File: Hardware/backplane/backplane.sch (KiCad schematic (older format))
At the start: 45 parts, among them J1 USB_B_Micro, SW1 SW_SPST, U2 MAX811SEUS-T, U3 MAX811SEUS-T, U4 PAL24, X1 CXO_DIP8

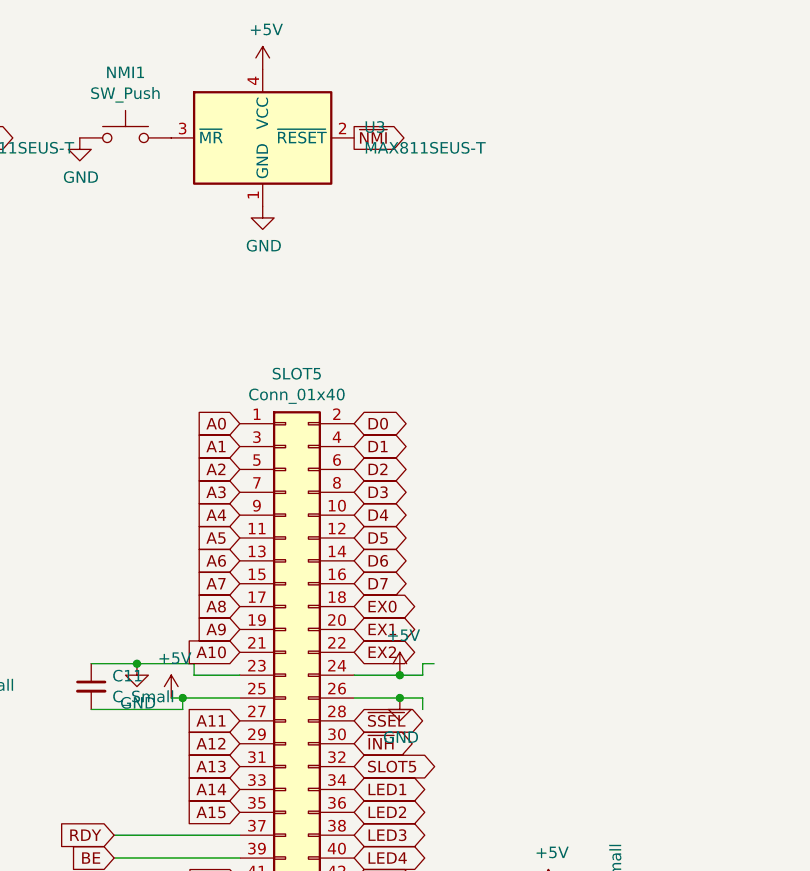
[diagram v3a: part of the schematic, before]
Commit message: Add resistor between output of NMI MAX811 and NMI line to enable NMI to be controlled from the bus
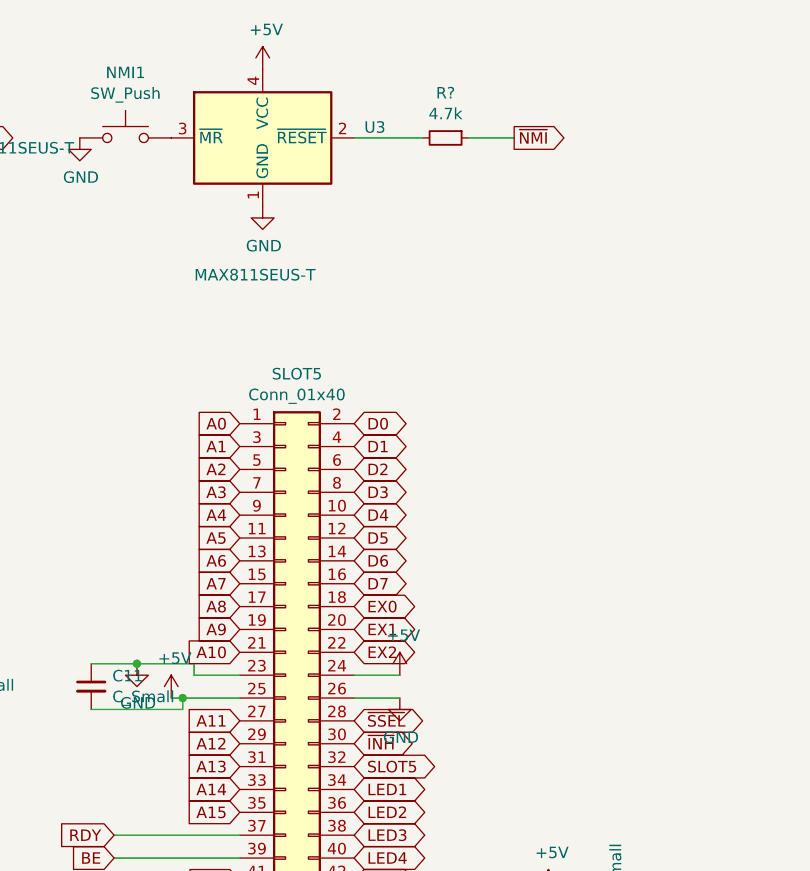
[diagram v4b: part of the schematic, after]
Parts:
- added R?: 4.7k, Resistor_SMD:R_0805_2012Metric_Pad1.15x1.40mm_HandSolder, symbol Device:R_Small
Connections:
- wire segments 123 -> 120
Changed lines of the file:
@@
 Text GLabel 8200 4550 0    50   Input ~ 0
 ~IRQ~
-Wire Wire Line
-	9600 3400 9550 3400
-Wire Wire Line
-	9550 3400 9550 3450
-Wire Wire Line
-	9550 3450 9450 3450
-Connection ~ 9450 3450
-Wire Wire Line
-	9550 3600 9550 3550
-Wire Wire Line
-	9550 3550 9450 3550
-Connection ~ 9450 3550
 $Comp
 L Device:C_Small C11
@@
 P 8850 1100
 F 0 "U3" H 9294 1146 50  0000 L CNN
-F 1 "MAX811SEUS-T" H 9294 1055 50  0000 L CNN
+F 1 "MAX811SEUS-T" H 8550 500 50  0000 L CNN
 F 2 "Package_TO_SOT_SMD:SOT-143" H 8950 800 50  0001 L CNN
 F 3 "https://datasheets.maximintegrated.com/en/ds/MAX811-MAX812.pdf" H 8500 400 50  0001 C CNN
@@
 	1    0    0    -1
 $EndComp
-Text GLabel 9250 1100 2    50   Output ~ 0
+Text GLabel 9950 1100 2    50   Output ~ 0
 ~NMI~
 Text GLabel 7450 1100 2    50   Output ~ 0
@@
 Wire Wire Line
 	1550 1100 2050 1100
+Wire Wire Line
+	9950 1100 9750 1100
+Wire Wire Line
+	9550 1100 9250 1100
+$Comp
+L Device:R_Small R?
+U 1 1 60052F9C
+P 9650 1100
+F 0 "R?" V 9454 1100 50  0000 C CNN
+F 1 "4.7k" V 9545 1100 50  0000 C CNN
+F 2 "Resistor_SMD:R_0805_2012Metric_Pad1.15x1.40mm_HandSolder" H 9650 1100 50  0001 C CNN
+F 3 "~" H 9650 1100 50  0001 C CNN
+	1    9650 1100
+	0    1    1    0
+$EndComp
 $EndSCHEMATC

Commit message: change resistor
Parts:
- gave numbers to parts that had none: 1
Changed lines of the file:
@@
 	9550 1100 9250 1100
 $Comp
-L Device:R_Small R?
+L Device:R_Small R16
 U 1 1 60052F9C
 P 9650 1100
-F 0 "R?" V 9454 1100 50  0000 C CNN
+F 0 "R16" V 9454 1100 50  0000 C CNN
 F 1 "4.7k" V 9545 1100 50  0000 C CNN
 F 2 "Resistor_SMD:R_0805_2012Metric_Pad1.15x1.40mm_HandSolder" H 9650 1100 50  0001 C CNN

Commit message: Add backplane gerbers
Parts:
- removed C2: C_Small, Capacitor_SMD:C_1206_3216Metric_Pad1.42x1.75mm_HandSolder, symbol Device:C_Small
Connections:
- wire segments 120 -> 114
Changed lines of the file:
@@
 ~IRQ~
-$Comp
-L Device:C_Small C2
-U 1 1 5FD8A65F
-P 3150 3500
-F 0 "C2" H 3242 3546 50  0000 L CNN
-F 1 "C_Small" H 3242 3455 50  0000 L CNN
-F 2 "Capacitor_SMD:C_1206_3216Metric_Pad1.42x1.75mm_HandSolder" H 3150 3500 50  0001 C CNN
-F 3 "~" H 3150 3500 50  0001 C CNN
-	1    3150 3500
-	1    0    0    -1
-$EndComp
-Wire Wire Line
-	3150 3400 3100 3400
-Wire Wire Line
-	3100 3400 3100 3450
-Wire Wire Line
-	3100 3450 3000 3450
-Connection ~ 3000 3450
-Wire Wire Line
-	3150 3600 3100 3600
-Wire Wire Line
-	3100 3600 3100 3550
-Wire Wire Line
-	3100 3550 3000 3550
-Connection ~ 3000 3550
 $Comp
 L Device:C_Small C1
@@
 	1    0    0    -1
 $EndComp
-Text GLabel 10700 5050 2    50   Output ~ 0
+Text GLabel 10700 5850 2    50   Output ~ 0
 CLK
 Text GLabel 4950 3650 2    50   BiDi ~ 0

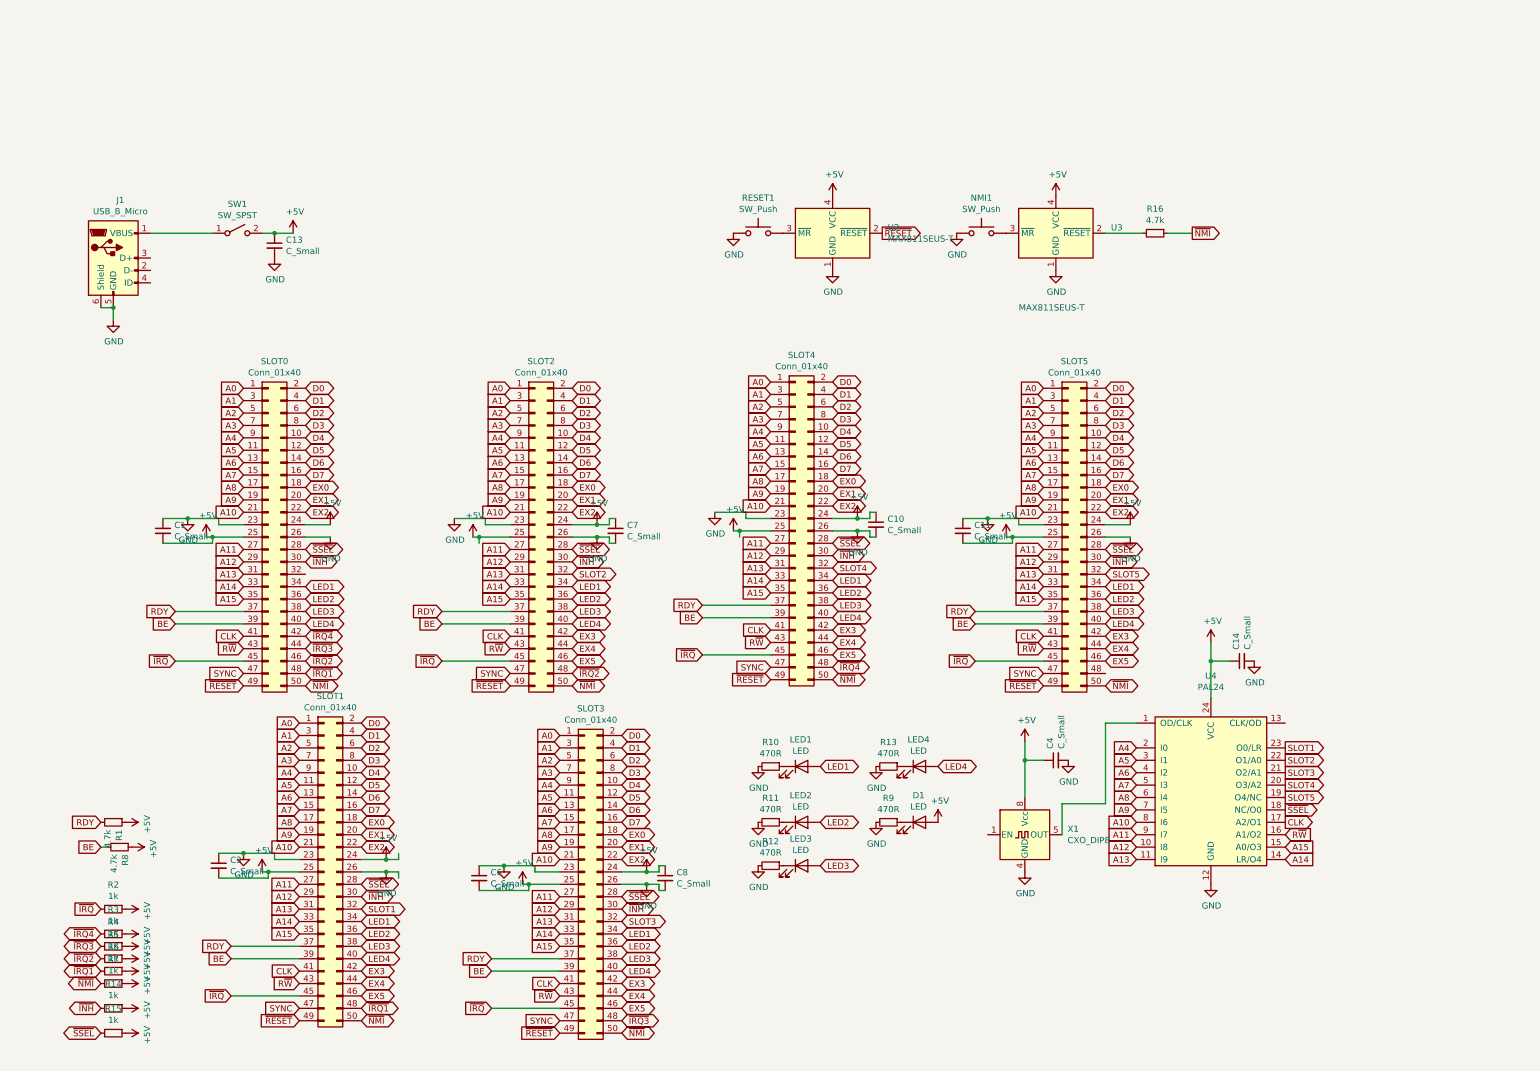
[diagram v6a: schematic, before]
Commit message: Add clock stretching with counter and slow clock request from peripherals.
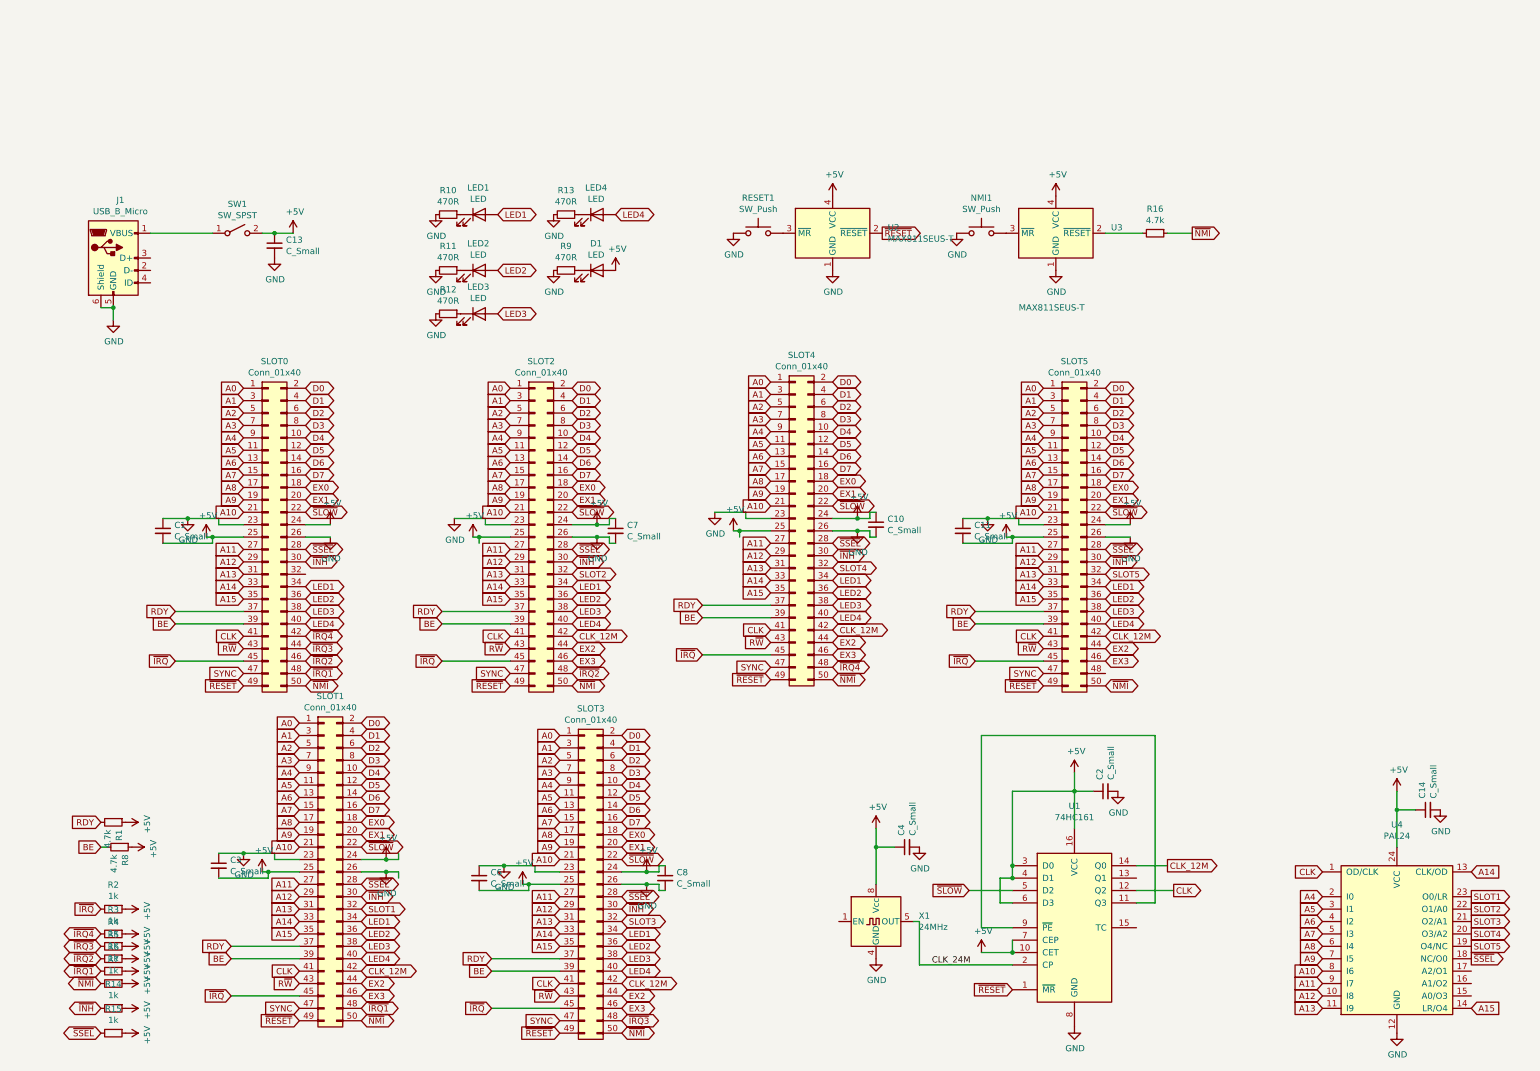
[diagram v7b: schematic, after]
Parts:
- added C2: C_Small, Capacitor_SMD:C_1206_3216Metric_Pad1.42x1.75mm_HandSolder, symbol Device:C_Small
- added U1: 74HC161, Package_DIP:DIP-16_W7.62mm_Socket, symbol 74xx:74LS161
- X1: value CXO_DIP8 -> 24MHz
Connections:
- net labels added: CLK_12M, CLK_24M, ~SLOW~
- net labels removed: EX4, EX5
- wire segments 114 -> 132
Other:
- moved on the sheet: C14, C4, D1, LED1, LED2, LED3, LED4, R10, R11, R12, R13, R9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

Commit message: each slot gets it's own slow signal
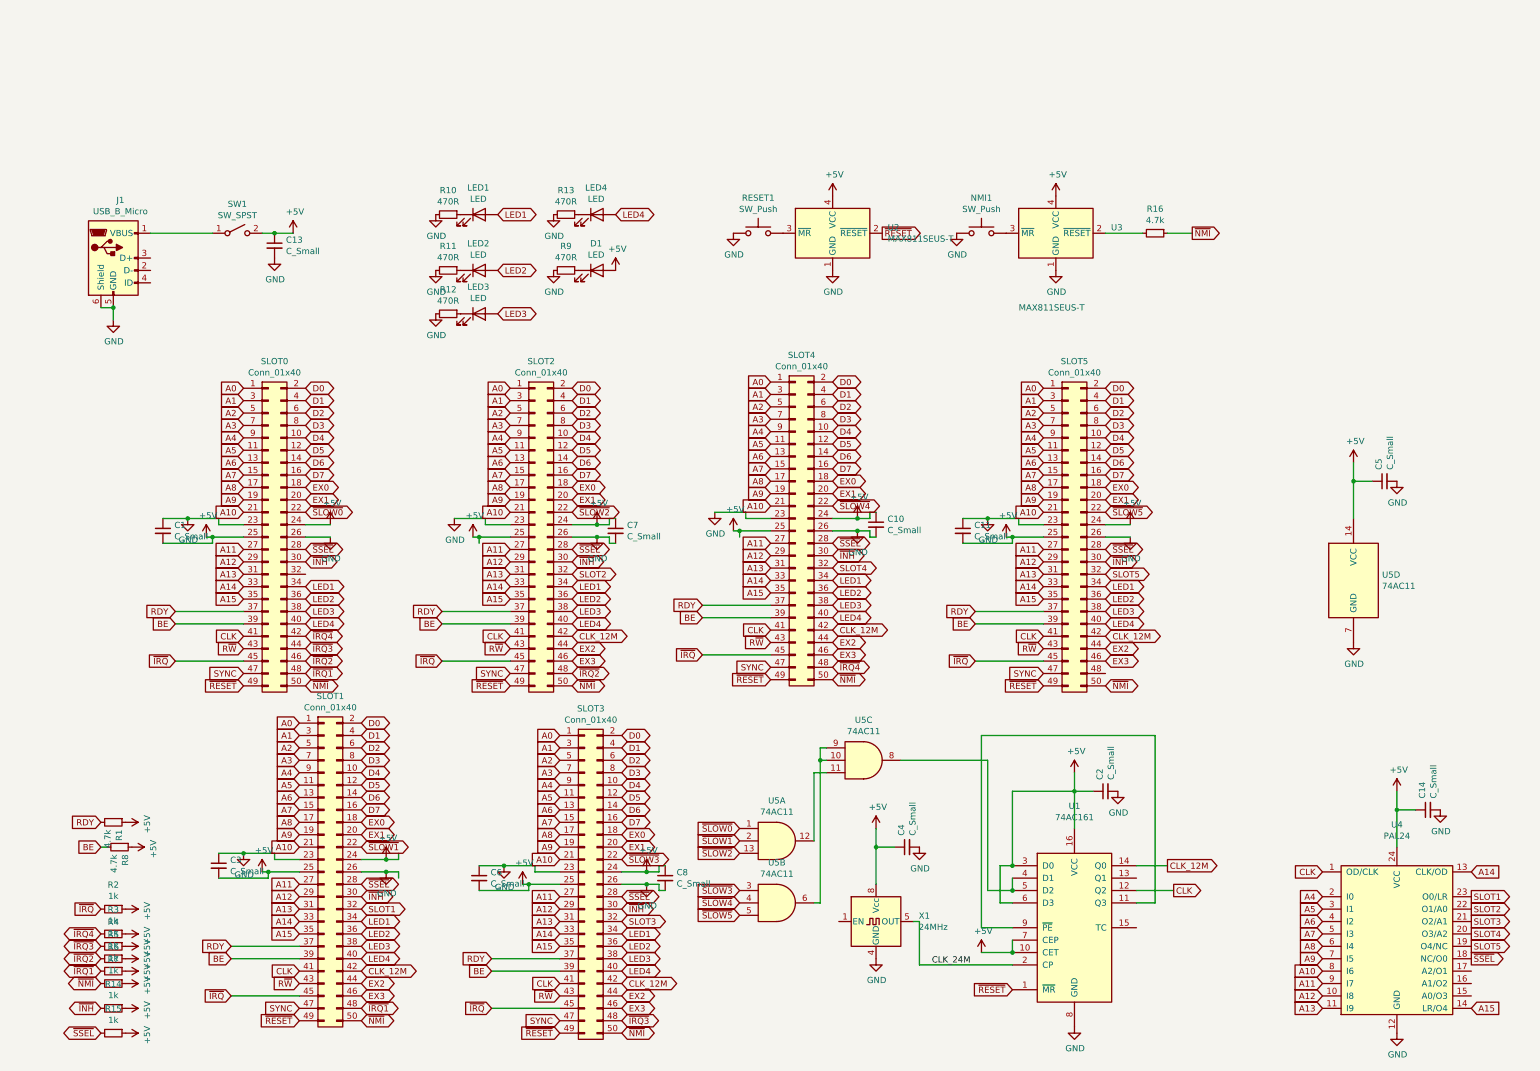
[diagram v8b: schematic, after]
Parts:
- added C5: C_Small, Capacitor_SMD:C_1206_3216Metric_Pad1.42x1.75mm_HandSolder, symbol Device:C_Small
- added U5: 74AC11, Package_SO:SOIC-14_3.9x8.7mm_P1.27mm, symbol 74xx:74LS11
- U1: value 74HC161 -> 74AC161; footprint Package_DIP:DIP-16_W7.62mm_Socket -> Package_SO:SOIC-16_3.9x9.9mm_P1.27mm
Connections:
- net labels added: ~SLOW0~, ~SLOW1~, ~SLOW2~, ~SLOW3~, ~SLOW4~, ~SLOW5~
- net labels removed: ~SLOW~
- wire segments 132 -> 144
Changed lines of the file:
@@
 EX1
 Text GLabel 4950 3350 2    50   BiDi ~ 0
-~SLOW~
+~SLOW2~
 Text GLabel 4950 3750 2    50   BiDi ~ 0
 ~INH~
@@
 LED4
 Text GLabel 2800 3350 2    50   BiDi ~ 0
-~SLOW~
+~SLOW0~
 Text GLabel 2800 3650 2    50   BiDi ~ 0
 ~SSEL~
 Text GLabel 7050 3300 2    50   BiDi ~ 0
-~SLOW~
+~SLOW4~
 Text GLabel 7050 3700 2    50   BiDi ~ 0
 ~INH~
@@
 SLOT4
 Text GLabel 9250 3350 2    50   BiDi ~ 0
-~SLOW~
+~SLOW5~
 Text GLabel 9250 3750 2    50   BiDi ~ 0
 ~INH~
@@
 SLOT5
 Text GLabel 5350 6150 2    50   BiDi ~ 0
-~SLOW~
+~SLOW3~
 Text GLabel 5350 6550 2    50   BiDi ~ 0
 ~INH~
@@
 SLOT3
 Text GLabel 3250 6050 2    50   BiDi ~ 0
-~SLOW~
+~SLOW1~
 Text GLabel 3250 6450 2    50   BiDi ~ 0
 ~INH~
@@
 P 9000 6700
 F 0 "U1" H 9000 7681 50  0000 C CNN
-F 1 "74HC161" H 9000 7590 50  0000 C CNN
-F 2 "Package_DIP:DIP-16_W7.62mm_Socket" H 9000 6700 50  0001 C CNN
+F 1 "74AC161" H 9000 7590 50  0000 C CNN
+F 2 "Package_SO:SOIC-16_3.9x9.9mm_P1.27mm" H 9000 6700 50  0001 C CNN
 F 3 "http://www.ti.com/lit/gpn/sn74LS163" H 9000 6700 50  0001 C CNN
 	1    9000 6700
@@
 	9500 6400 9800 6400
 Wire Wire Line
-	8500 6300 8500 6200
-Wire Wire Line
 	8500 5600 9000 5600
-Connection ~ 8500 6200
 Wire Wire Line
 	8500 6200 8500 5600
@@
 	8500 6500 8400 6500
 Wire Wire Line
-	8400 6500 8400 6300
-Wire Wire Line
-	8400 6300 8500 6300
-Connection ~ 8500 6300
-Text GLabel 8150 6400 0    50   Input ~ 0
-~SLOW~
-Wire Wire Line
-	8500 6400 8150 6400
+	8500 6400 8300 6400
 Text GLabel 7050 4400 2    50   BiDi ~ 0
 EX2
@@
 Text GLabel 3250 7250 2    50   BiDi ~ 0
 EX3
+Text GLabel 6300 5900 0    50   Input ~ 0
+~SLOW0~
+Text GLabel 6300 6000 0    50   Input ~ 0
+~SLOW1~
+Text GLabel 6300 6100 0    50   Input ~ 0
+~SLOW2~
+Text GLabel 6300 6400 0    50   Input ~ 0
+~SLOW3~
+Text GLabel 6300 6500 0    50   Input ~ 0
+~SLOW4~
+Text GLabel 6300 6600 0    50   Input ~ 0
+~SLOW5~
+Wire Wire Line
+	8300 5350 8300 6400
+$Comp
+L power:+5V #PWR0160
+U 1 1 5FFEA08F
+P 11250 2950
+F 0 "#PWR0160" H 11250 2800 50  0001 C CNN
+F 1 "+5V" H 11265 3123 50  0000 C CNN
+F 2 "" H 11250 2950 50  0001 C CNN
+F 3 "" H 11250 2950 50  0001 C CNN
+	1    11250 2950
+	1    0    0    -1
+$EndComp
+Wire Wire Line
+	11250 3400 11250 3100
+$Comp
+L Device:C_Small C5
+U 1 1 5FFEA096
+P 11500 3100
+F 0 "C5" H 11592 3146 50  0000 L CNN
+F 1 "C_Small" H 11592 3055 50  0000 L CNN
+F 2 "Capacitor_SMD:C_1206_3216Metric_Pad1.42x1.75mm_HandSolder" H 11500 3100 50  0001 C CNN
+F 3 "~" H 11500 3100 50  0001 C CNN
+	1    11500 3100
+	0    -1   -1   0
+$EndComp
+Wire Wire Line
+	11400 3100 11250 3100
+Connection ~ 11250 3100
+Wire Wire Line
+	11250 3100 11250 2950
+$Comp
+L power:GND #PWR0161
+U 1 1 5FFEA09F
+P 11600 3100
+F 0 "#PWR0161" H 11600 2850 50  0001 C CNN
+F 1 "GND" H 11605 2927 50  0000 C CNN
+F 2 "" H 11600 3100 50  0001 C CNN
+F 3 "" H 11600 3100 50  0001 C CNN
+	1    11600 3100
+	1    0    0    -1
+$EndComp
+$Comp
+L power:GND #PWR0162
+U 1 1 5FFF04AD
+P 11250 4400
+F 0 "#PWR0162" H 11250 4150 50  0001 C CNN
+F 1 "GND" H 11255 4227 50  0000 C CNN
+F 2 "" H 11250 4400 50  0001 C CNN
+F 3 "" H 11250 4400 50  0001 C CNN
+	1    11250 4400
+	1    0    0    -1
+$EndComp
+Wire Wire Line
+	8400 6500 8400 6200
+Wire Wire Line
+	8400 6200 8500 6200
+Connection ~ 8500 6200
+Wire Wire Line
+	8500 6300 8500 6400
+Connection ~ 8500 6400
+$Comp
+L 74xx:74LS11 U5
+U 1 1 6002FB92
+P 6600 6000
+F 0 "U5" H 6600 6325 50  0000 C CNN
+F 1 "74AC11" H 6600 6234 50  0000 C CNN
+F 2 "Package_SO:SOIC-14_3.9x8.7mm_P1.27mm" H 6600 6000 50  0001 C CNN
+F 3 "http://www.ti.com/lit/gpn/sn74LS11" H 6600 6000 50  0001 C CNN
+	1    6600 6000
+	1    0    0    -1
+$EndComp
+$Comp
+L 74xx:74LS11 U5
+U 2 1 600332A1
+P 6600 6500
+F 0 "U5" H 6600 6825 50  0000 C CNN
+F 1 "74AC11" H 6600 6734 50  0000 C CNN
+F 2 "Package_SO:SOIC-14_3.9x8.7mm_P1.27mm" H 6600 6500 50  0001 C CNN
+F 3 "http://www.ti.com/lit/gpn/sn74LS11" H 6600 6500 50  0001 C CNN
+	2    6600 6500
+	1    0    0    -1
+$EndComp
+$Comp
+L 74xx:74LS11 U5
+U 3 1 60036171
+P 7300 5350
+F 0 "U5" H 7300 5675 50  0000 C CNN
+F 1 "74AC11" H 7300 5584 50  0000 C CNN
+F 2 "Package_SO:SOIC-14_3.9x8.7mm_P1.27mm" H 7300 5350 50  0001 C CNN
+F 3 "http://www.ti.com/lit/gpn/sn74LS11" H 7300 5350 50  0001 C CNN
+	3    7300 5350
+	1    0    0    -1
+$EndComp
+$Comp
+L 74xx:74LS11 U5
+U 4 1 60038B35
+P 11250 3900
+F 0 "U5" H 11480 3946 50  0000 L CNN
+F 1 "74AC11" H 11480 3855 50  0000 L CNN
+F 2 "Package_SO:SOIC-14_3.9x8.7mm_P1.27mm" H 11250 3900 50  0001 C CNN
+F 3 "http://www.ti.com/lit/gpn/sn74LS11" H 11250 3900 50  0001 C CNN
+	4    11250 3900
+	1    0    0    -1
+$EndComp
+Wire Wire Line
+	6900 6500 6950 6500
+Wire Wire Line
+	7600 5350 8300 5350
+Wire Wire Line
+	6900 6000 6900 5450
+Wire Wire Line
+	6900 5450 7000 5450
+Wire Wire Line
+	6950 6500 6950 5350
+Wire Wire Line
+	6950 5250 7000 5250
+Wire Wire Line
+	7000 5350 6950 5350
+Connection ~ 6950 5350
+Wire Wire Line
+	6950 5350 6950 5250
 $EndSCHEMATC
